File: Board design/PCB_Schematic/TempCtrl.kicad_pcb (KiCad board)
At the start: 4 copper layers, 80 x 100 mm, 153 parts, among them CON1 BARREL_JACK, IC1 ATMEGA328P-A, P1 233-2977, P2 820-8104, P3 RS485, P4 USB_OTG, P5 ICSP, P6 ADC breakout, SW1 DISABLE_COMMS, SW2 SWITCH_INV, U1 LM7805, U10 INA330, U11 ISO7242, U12 FT232RL, U13 ADS1262, U14 AD8639, U15 DAC8564, U16 AD8639, U17 DAC8564, U2 TMA0505S, U3 ADuM7642CRQZ, U4 ISO3088, U5 OPA548, U6 OPA548, U7 OPA548, U8 OPA548, U9 INA330, X1 TSX-3225 X1E0000210013

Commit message: Update to fix latex KiCad breakages
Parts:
- W1, W2, W3, W4: footprint Measurement_Points:Test_Point_2Pads -> Custom:Test_Point_2Pads_shorted

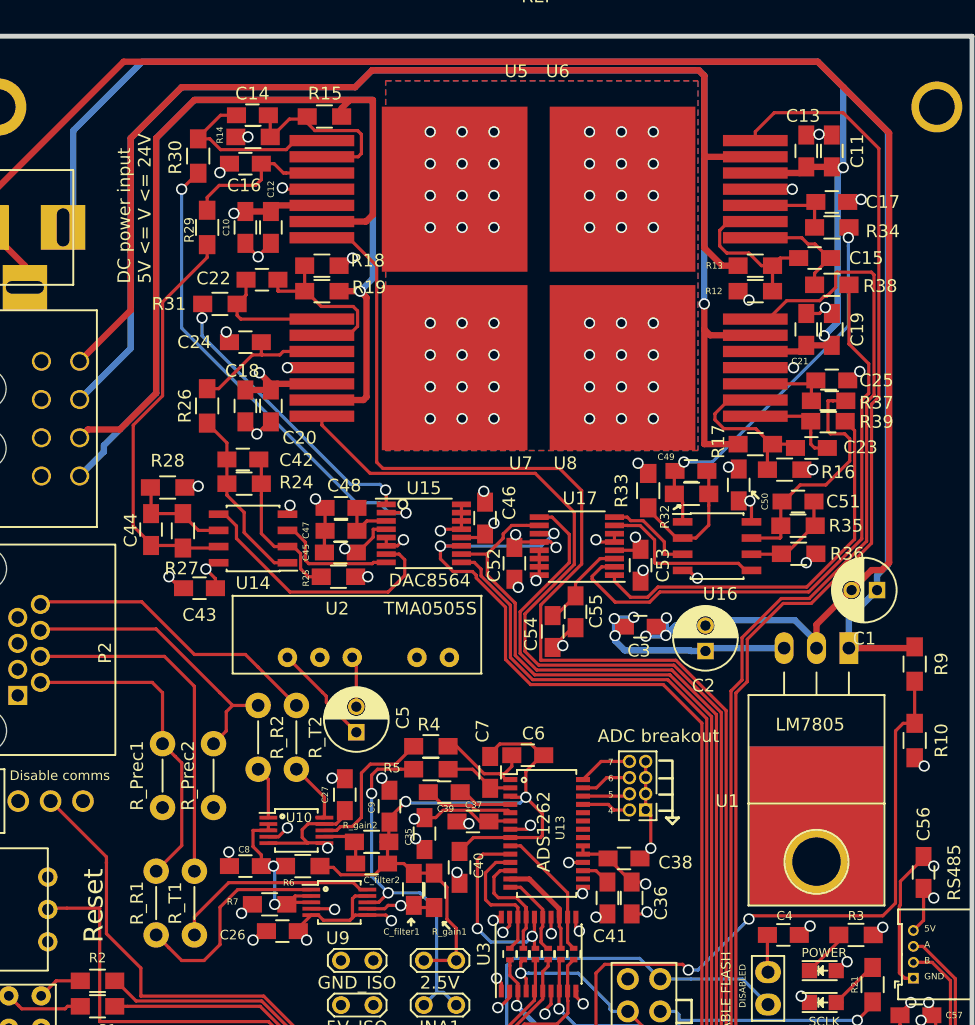
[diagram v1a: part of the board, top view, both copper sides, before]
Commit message: Update PCB, removing some but not all of the courtyard failures
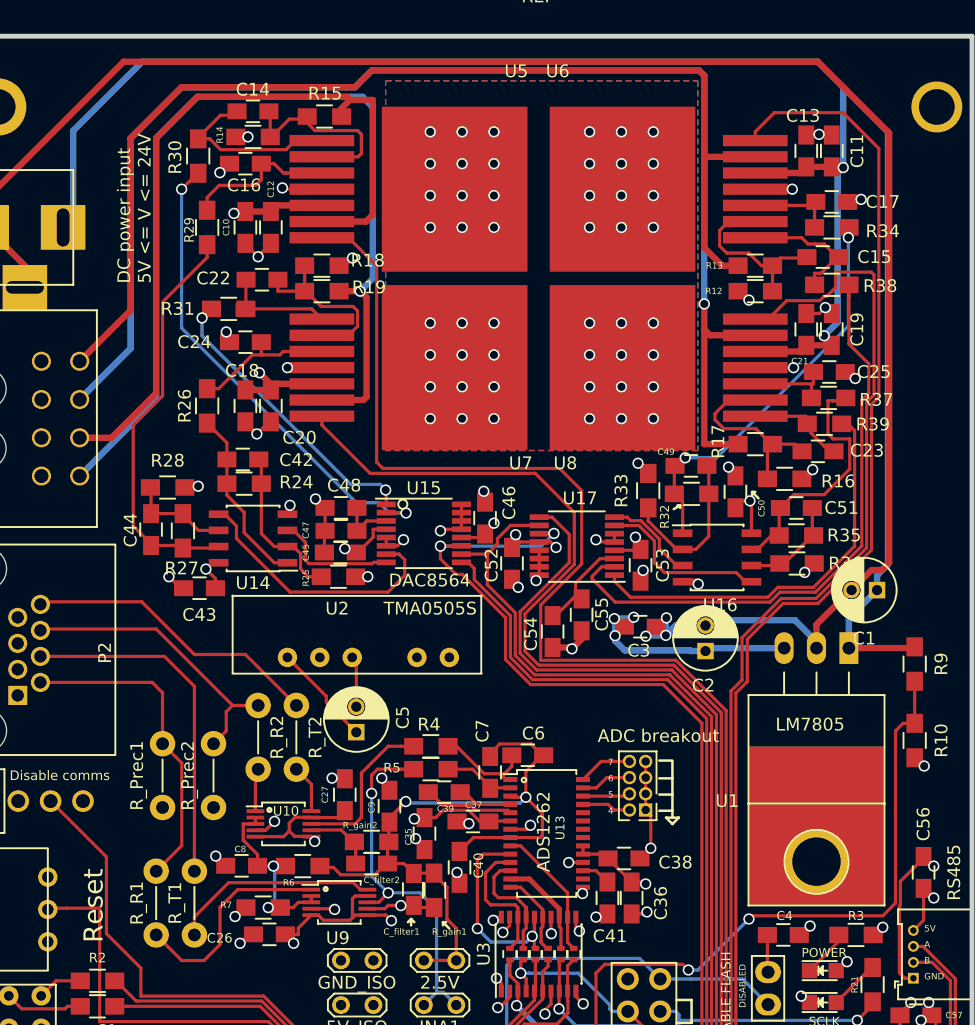
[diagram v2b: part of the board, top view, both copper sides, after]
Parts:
- moved U10 1.14 mm to (191.0, 96.8)
- moved C26 1.05 mm to (189.9, 105.5)
- moved U16 0.89 mm to (225.0, 75.9)
- moved R31 0.79 mm to (186.7, 56.4)
- moved R36 0.77 mm to (231.3, 76.4)
- moved R35 0.77 mm to (231.2, 74.2)
- moved R16 0.72 mm to (230.3, 69.7)
- moved C25 0.69 mm to (233.8, 61.3)
- moved C15 0.65 mm to (233.3, 52.3)
- moved C50 0.60 mm to (226.4, 70.7)
- moved C23 0.58 mm to (232.9, 67.6)
- moved R7 0.57 mm to (189.4, 103.4)
- moved C55 0.53 mm to (214.4, 80.4)
- moved C51 0.52 mm to (231.2, 72.0)
- moved C49 0.39 mm to (222.9, 68.7)
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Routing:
- net /ANALOG_+5: track 48.1 -> 50.3 mm
- net Net-(C49-Pad2): track 10.5 -> 12.5 mm
- net Net-(C_filter2-Pad1): track 4.76 -> 6.58 mm
- net /OPA3_IN+: track 11.6 -> 12.7 mm
- net /INA330_interface2/I_BIAS_T: track 6.21 -> 5.28 mm
- net +5V: track 58.9 -> 59.8 mm
- net /INA_ERROR_2: track 11.9 -> 12.7 mm
- net /INA330_interface2/I_BIAS_R: track 4.63 -> 3.88 mm
- net /OPA4_IN-: track 15.5 -> 16.3 mm
- net Net-(C49-Pad1): track 30.3 -> 31.0 mm
- net /MOSI: track 97.2 -> 96.6 mm
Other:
- board text added: "Sorry about all the DRC failures for intersecting courtyards: when I made this board Kicad didn't check for these!"

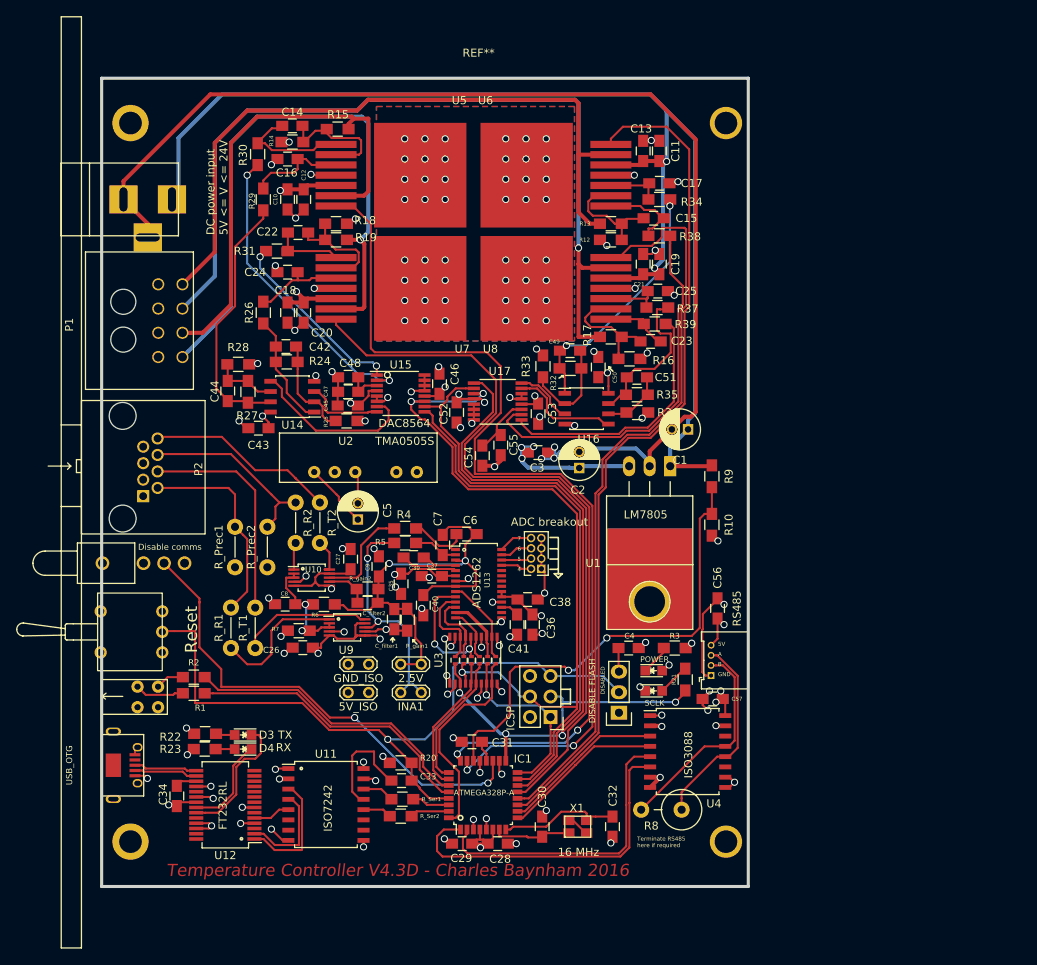
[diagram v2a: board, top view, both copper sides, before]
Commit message: Add more testpoints and change to the single hoop style
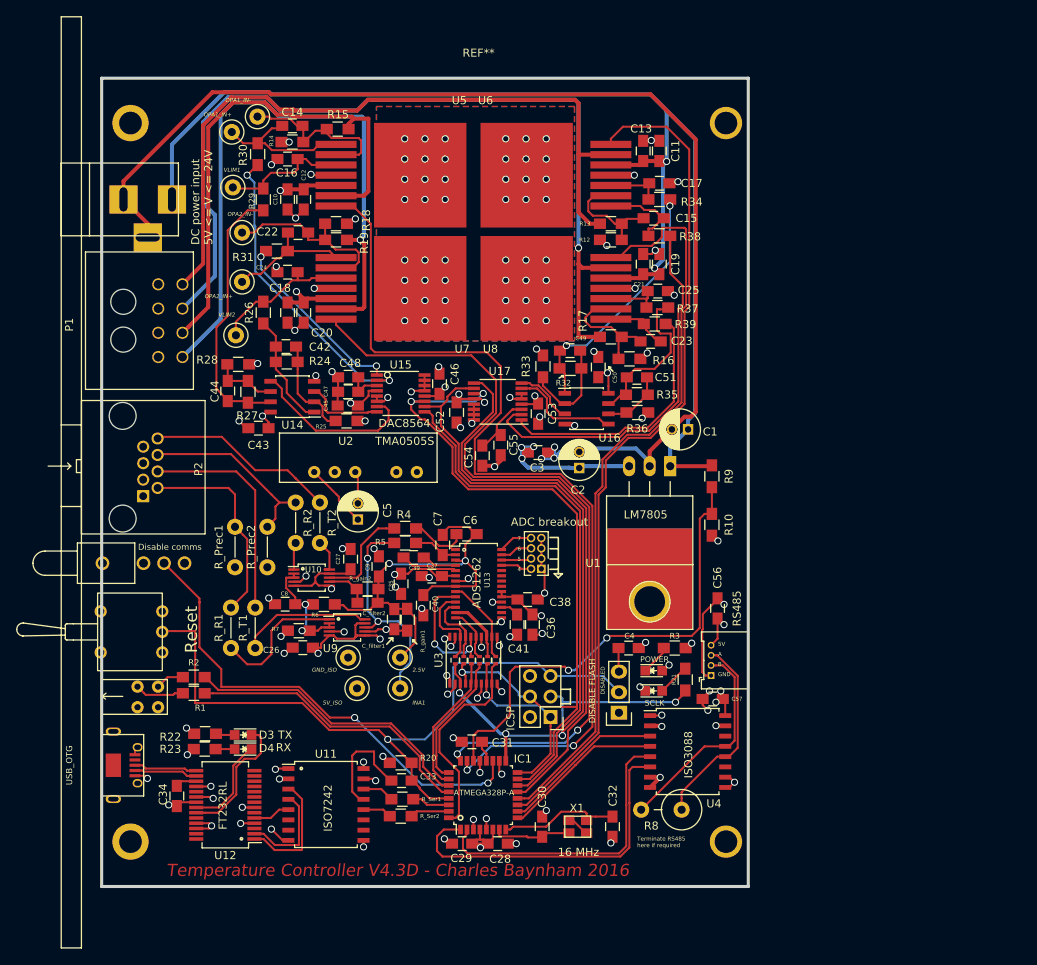
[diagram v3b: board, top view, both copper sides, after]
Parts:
- added W10: VLIM2, TestPoint:TestPoint_Loop_D2.50mm_Drill1.0mm, F.Cu at (181.6, 66.8)
- added W5: OPA1_IN+, TestPoint:TestPoint_Loop_D2.50mm_Drill1.0mm, F.Cu at (181.1, 41.7)
- added W6: OPA1_IN-, TestPoint:TestPoint_Loop_D2.50mm_Drill1.0mm, F.Cu at (184.3, 39.8)
- added W7: VLIM1, TestPoint:TestPoint_Loop_D2.50mm_Drill1.0mm, F.Cu at (181.2, 48.5)
- added W8: OPA2_IN+, TestPoint:TestPoint_Loop_D2.50mm_Drill1.0mm, F.Cu at (182.4, 60.2)
- added W9: OPA2_IN-, TestPoint:TestPoint_Loop_D2.50mm_Drill1.0mm, F.Cu at (182.4, 54.1)
- W1, W2, W3, W4: footprint Custom:Test_Point_2Pads_shorted -> TestPoint:TestPoint_Loop_D2.50mm_Drill1.0mm
- moved W4 1.21 mm to (196.6, 110.5)
- moved W3 0.82 mm to (201.9, 106.7)
- moved W2 0.82 mm to (195.5, 106.7)
- moved W1 0.51 mm to (201.9, 110.5)
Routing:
- net /OPA2_IN-: track 14.1 -> 23.1 mm
- net /OPA2_IN+: track 9.49 -> 16.7 mm
- net /VLIM2: track 11.3 -> 17.4 mm
- net /OPA1_IN-: track 17.2 -> 23.2 mm
- net /C4+_OUT: track 106.0 -> 110.9 mm
- net /VLIM1: track 12.2 -> 16.1 mm
- net /C2+_OUT: track 76.3 -> 80.1 mm
- net /OPA1_IN+: track 16.2 -> 20.0 mm
- net /C3+_OUT: track 87.3 -> 90.8 mm
- net /ADC_2.5_REF: track 56.7 -> 53.8 mm
- net /C1+_OUT: track 60.7 -> 63.5 mm
- net /INA_ERROR_1: track 29.4 -> 27.1 mm
- net Net-(C44-Pad1): track 32.0 -> 33.1 mm

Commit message: Start PCB
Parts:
- added R11: R_Small, Resistor_SMD:R_0805_2012Metric_Pad1.15x1.40mm_HandSolder, F.Cu at (268.0, 116.8)
- added R40: R_Small, Resistor_SMD:R_0805_2012Metric_Pad1.15x1.40mm_HandSolder, F.Cu at (276.9, 110.2)
- added R41: R_Small, Resistor_SMD:R_0805_2012Metric_Pad1.15x1.40mm_HandSolder, F.Cu at (272.7, 116.8)
- added R42: R_Small, Resistor_SMD:R_0805_2012Metric_Pad1.15x1.40mm_HandSolder, F.Cu at (276.9, 113.1)
- added U18: 74LS125, Package_SO:TSSOP-14_4.4x5mm_P0.65mm, F.Cu at (225.0, 121.4)
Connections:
- IC1 pad 11: /E/S3 -> /ES4_IN
- IC1 pad 12: /E/S4 -> /ES3_IN
- IC1 pad 23: /E/S1 -> /ES1_IN
- IC1 pad 24: /E/S2 -> /ES2_IN
- U5 pad 7: /E/S1 -> /ES1_OUT
- U6 pad 7: /E/S3 -> /ES3_OUT
- U7 pad 7: /E/S2 -> /ES2_OUT
- U8 pad 7: /E/S4 -> /ES4_OUT
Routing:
- net /E/S1: track 114.6 -> 0.00 mm, vias 2 -> 0
- net /E/S3: track 104.3 -> 0.00 mm
- net /E/S2: track 98.5 -> 0.00 mm, vias 2 -> 0
- net /E/S4: track 96.8 -> 0.00 mm
- net /ES1_OUT: track 0.00 -> 95.8 mm
- net /ES3_OUT: track 0.00 -> 90.6 mm
- net /ES4_OUT: track 0.00 -> 83.8 mm
- net /ES2_OUT: track 0.00 -> 80.8 mm
- net /ES2_IN: track 0.00 -> 21.5 mm, vias 0 -> 2
- net /ES1_IN: track 0.00 -> 20.9 mm, vias 0 -> 2
- net Earth_Clean: track 233.2 -> 244.3 mm, vias 102 -> 105
- net /ES3_IN: track 0.00 -> 7.07 mm
- net /ES4_IN: track 0.00 -> 6.55 mm
- net /RS485_RE: track 20.1 -> 23.3 mm
- net /RS485_R: track 20.3 -> 23.3 mm
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
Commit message: Add to board
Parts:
- moved R41 56.1 mm to (221.0, 117.3), turned to 180 degrees
- moved R42 53.6 mm to (219.5, 122.4), turned to 270 degrees
- moved R11 47.3 mm to (230.1, 117.3), turned to 270 degrees
- moved R40 40.9 mm to (227.1, 117.3)
- moved C37 0.36 mm to (205.5, 96.6)
- renumbered R40 to R11, R11 to R40, R42 to R41, R41 to R42
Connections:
- IC1 pad 11: /ES4_IN -> /ES1_IN
- IC1 pad 12: /ES3_IN -> /ES2_IN
- IC1 pad 23: /ES1_IN -> /ES4_IN
- IC1 pad 24: /ES2_IN -> /ES3_IN
- R11 pad 2: /ES2_IN -> /ES4_IN
- R40 pad 2: /ES1_IN -> /ES3_IN
- R41 pad 2: /ES4_IN -> /ES2_IN
- R42 pad 2: /ES3_IN -> /ES1_IN
- U18 pad 1: /ES1_IN -> /ES4_IN
- U18 pad 10: /ES3_IN -> /ES2_IN
- U18 pad 11: /ES4_OUT -> /ES1_OUT
- U18 pad 13: /ES4_IN -> /ES1_IN
- U18 pad 3: /ES1_OUT -> /ES4_OUT
- U18 pad 4: /ES2_IN -> /ES3_IN
- U18 pad 6: /ES2_OUT -> /ES3_OUT
- U18 pad 8: /ES3_OUT -> /ES2_OUT
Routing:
- net /ES4_IN: track 6.55 -> 27.4 mm, vias 0 -> 2
- net /ES3_IN: track 7.07 -> 26.7 mm, vias 0 -> 2
- net /ES1_IN: track 20.9 -> 6.55 mm, vias 2 -> 0
- net /ES2_IN: track 21.5 -> 11.9 mm, vias 2 -> 0
- net /ES4_OUT: track 83.8 -> 93.2 mm
- net /ES1_OUT: track 95.8 -> 104.3 mm
- net /ES3_OUT: track 90.6 -> 97.4 mm
- net /ES2_OUT: track 80.8 -> 86.3 mm
- net Earth_Clean: track 244.3 -> 247.7 mm, vias 105 -> 110
- net /SCLK: track 107.3 -> 106.5 mm
- net /DAC_CS1: track 65.4 -> 65.9 mm
- net /MISO: track 21.5 -> 22.1 mm

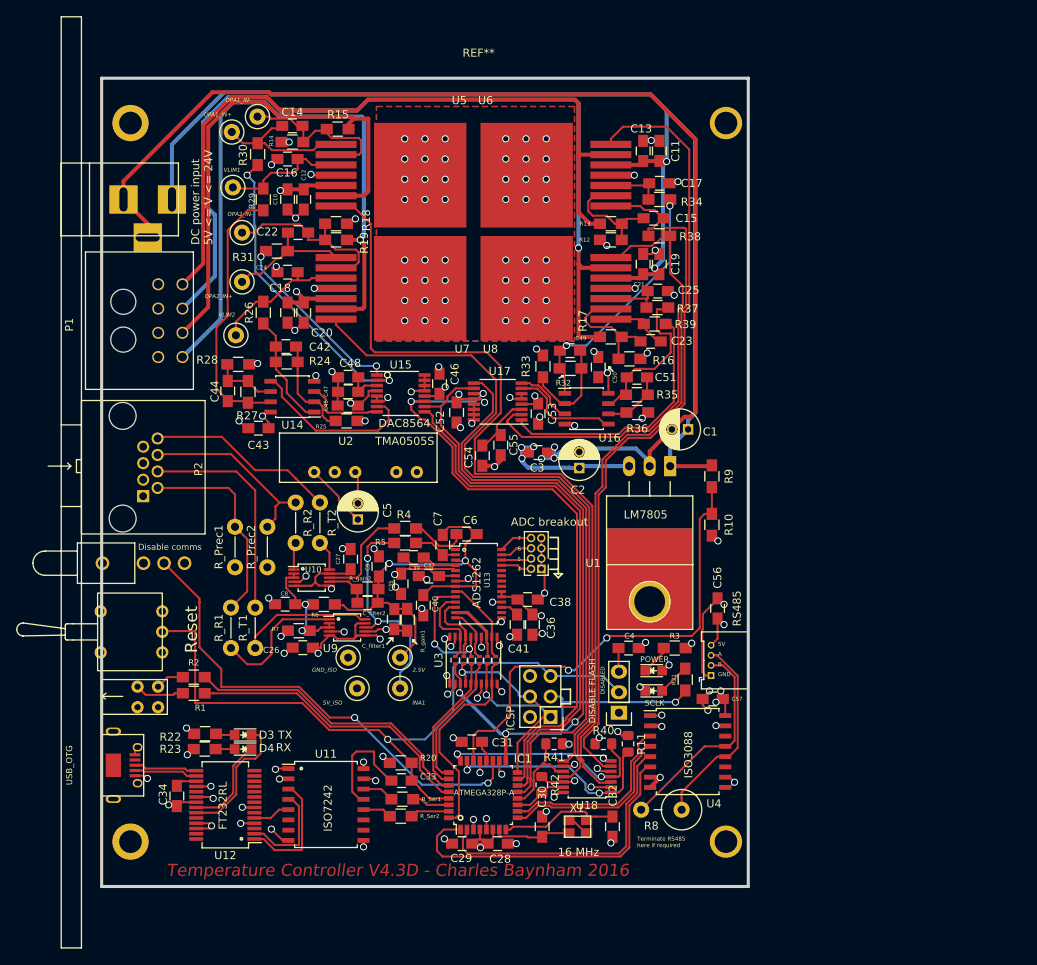
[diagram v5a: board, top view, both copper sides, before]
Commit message: Change to newer resistors with smaller courtyards
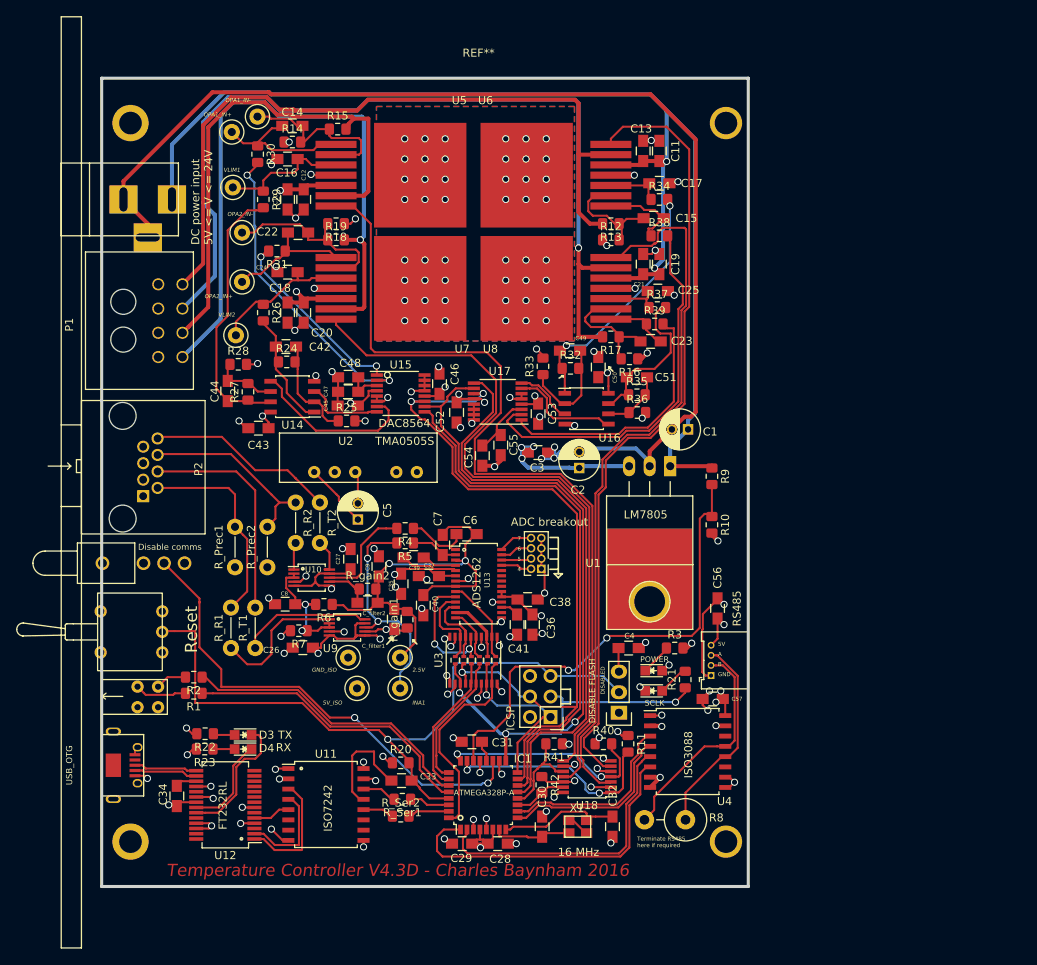
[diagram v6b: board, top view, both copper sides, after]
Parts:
- R1, R10, R12, R13, R14, R15, R16, R17, R18, R19, R2, R20, R21, R22, R23, R24, R25, R26, R27, R28, R29, R3, R30, R31, R32, R33, R34, R35, R36, R37, R38, R39, R4, R5, R6, R7, R9, R_Ser1, R_Ser2, R_gain1, R_gain2: footprint Resistors_SMD:R_0805_HandSoldering -> Resistor_SMD:R_0805_2012Metric_Pad1.15x1.40mm_HandSolder
- R8: footprint Resistors_ThroughHole:Resistor_Vertical_RM5mm -> Resistor_THT:R_Axial_DIN0516_L15.5mm_D5.0mm_P5.08mm_Vertical
- moved R8 3.24 mm to (237.2, 126.7)
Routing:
- net /RS485_B: track 27.0 -> 28.0 mm
- net /DACOutputs2/DAC_OUT_D: track 32.1 -> 32.7 mm
